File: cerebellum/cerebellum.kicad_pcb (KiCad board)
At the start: 4 copper layers, 95 x 56 mm, 30 parts, among them J1 GPIO, J2 MOTA, J3 MOTB, J4 MD_POW, J5 Conn_SPI, J6 Conn_UART, J7 Conn_I2C, J8 VBUS(OUT), J9 3V3(OUT), SW1 PULLUP, SW2 PULLDOWN, SW3 SW_SPDT, U2 POLOLU_TB6612_CARRIER, U3 HC-SR04

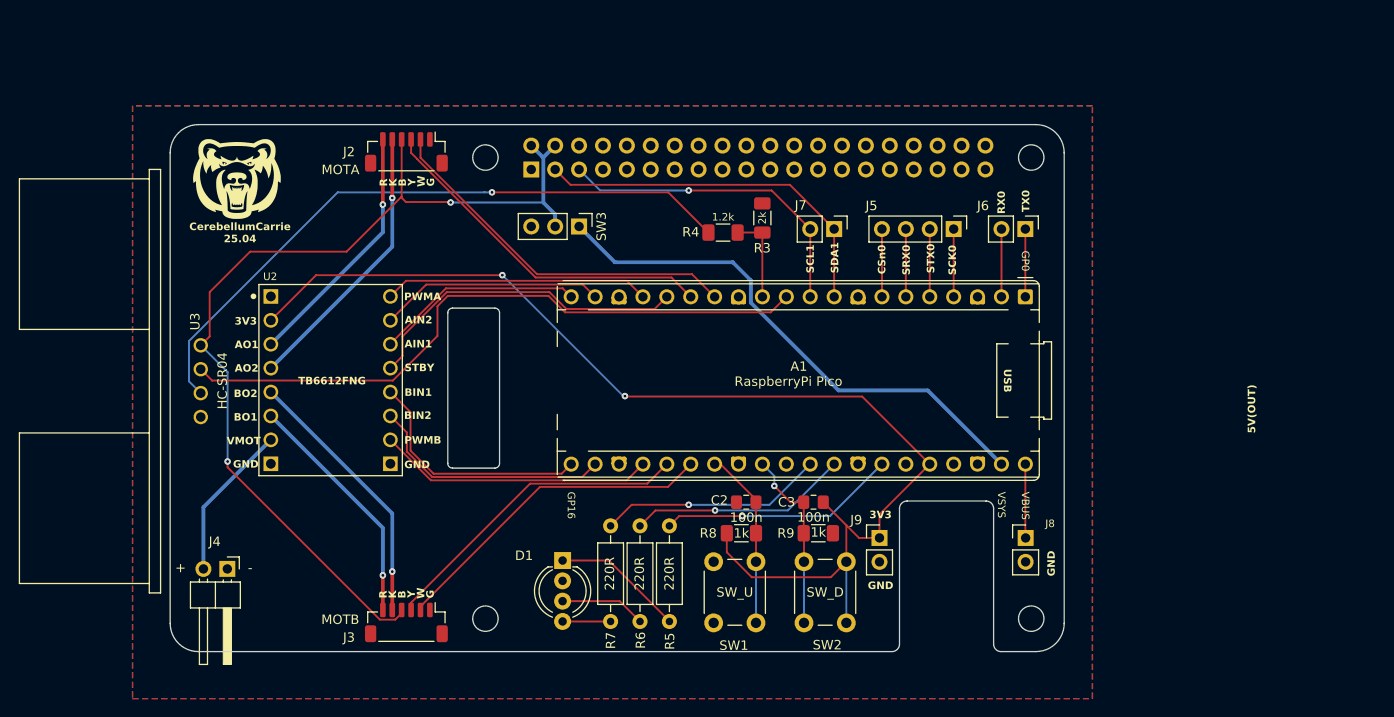
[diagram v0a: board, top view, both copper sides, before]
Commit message: update resistors and capacitors footprint to tht
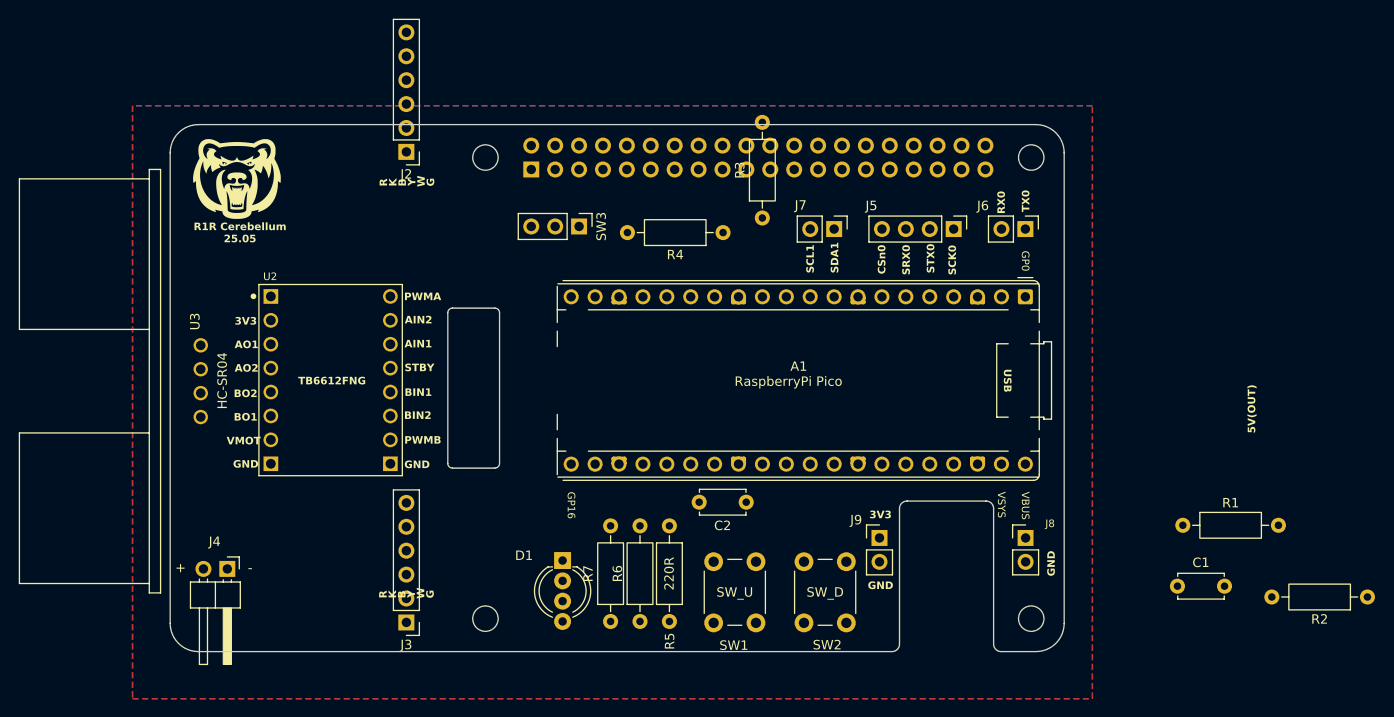
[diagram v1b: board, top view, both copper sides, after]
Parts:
- removed C3: 100n, Capacitor_SMD:C_0805_2012Metric_Pad1.18x1.45mm_HandSolder
- removed R8, R9: 1k, Resistor_SMD:R_1206_3216Metric_Pad1.30x1.75mm_HandSolder
- added C1: 100n, Capacitor_THT:C_Disc_D4.7mm_W2.5mm_P5.00mm, F.Cu at (177.0, 93.0)
- added R1: 1.2k, Resistor_THT:R_Axial_DIN0207_L6.3mm_D2.5mm_P10.16mm_Horizontal, F.Cu at (177.6, 86.6)
- added R2: 2k, Resistor_THT:R_Axial_DIN0207_L6.3mm_D2.5mm_P10.16mm_Horizontal, F.Cu at (197.2, 94.2)
- C2: footprint Capacitor_SMD:C_0805_2012Metric_Pad1.18x1.45mm_HandSolder -> Capacitor_THT:C_Disc_D4.7mm_W2.5mm_P5.00mm
- J2: value MOTA -> Conn_01x06_Pin; footprint Connector_JST:JST_SH_BM06B-SRSS-TB_1x06-1MP_P1.00mm_Vertical -> Connector_PinHeader_2.54mm:PinHeader_1x06_P2.54mm_Vertical
- J3: value MOTB -> Conn_01x06_Pin; footprint Connector_JST:JST_SH_BM06B-SRSS-TB_1x06-1MP_P1.00mm_Vertical -> Connector_PinHeader_2.54mm:PinHeader_1x06_P2.54mm_Vertical
- R3: value 2k -> 220R; footprint Resistor_SMD:R_1206_3216Metric_Pad1.30x1.75mm_HandSolder -> Resistor_THT:R_Axial_DIN0207_L6.3mm_D2.5mm_P10.16mm_Horizontal
- R4: value 1.2k -> 220R; footprint Resistor_SMD:R_1206_3216Metric_Pad1.30x1.75mm_HandSolder -> Resistor_THT:R_Axial_DIN0207_L6.3mm_D2.5mm_P10.16mm_Horizontal
- R6, R7: value 220R -> 1k
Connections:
- C2 pad 1: /SW_PU -> PICO3.3
- C2 pad 2: GND -> /SW_PD
- J2 pad 1: GND -> /AO1
- J2 pad 2: /AENC_W -> /AO2
- J2 pad 3: /AENC_Y -> +5V
- J2 pad 4: +5V -> /AENC_Y
- J2 pad 5: /AO2 -> /AENC_W
- J2 pad 6: /AO1 -> GND
- J3 pad 1: GND -> /BO1
- J3 pad 2: /BENC_W -> /BO2
- J3 pad 3: /BENC_Y -> +5V
- J3 pad 4: +5V -> /BENC_Y
- J3 pad 5: /BO2 -> /BENC_W
- J3 pad 6: /BO1 -> GND
- R3 pad 1: /ECHO -> Net-(D1-RA)
- R3 pad 2: GND -> /R_LED
- R4 pad 1: /ECHO -> Net-(D1-GA)
- R4 pad 2: Net-(U3-ECHO) -> /G_LED
- R5 pad 1: Net-(D1-RA) -> Net-(D1-BA)
- R5 pad 2: /R_LED -> /B_LED
- R6 pad 1: Net-(D1-GA) -> /SW_PU
- R6 pad 2: /G_LED -> PICO3.3
- R7 pad 1: Net-(D1-BA) -> GND
- R7 pad 2: /B_LED -> /SW_PD
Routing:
- net PICO3.3: track 124.8 -> 0.00 mm, vias 2 -> 0
- net +5V: track 103.6 -> 0.00 mm, vias 2 -> 0
- net /TRIG: track 69.7 -> 0.00 mm
- net Net-(U3-ECHO): track 69.6 -> 0.00 mm, vias 1 -> 0
- net VSYS: track 56.7 -> 0.00 mm
- net /SDA: track 39.5 -> 0.00 mm
- net /AENC_W: track 39.3 -> 0.00 mm
- net /AENC_Y: track 37.5 -> 0.00 mm
- net /BENC_W: track 35.4 -> 0.00 mm
- net /STBY: track 35.2 -> 0.00 mm
- net /SCL: track 34.4 -> 0.00 mm, vias 1 -> 0
- net /BENC_Y: track 34.0 -> 0.00 mm
- net /AO2: track 29.6 -> 0.00 mm, vias 1 -> 0
- net /PWMB: track 29.3 -> 0.00 mm
- net /BO2: track 28.5 -> 0.00 mm, vias 1 -> 0
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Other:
- board text added: "R1R Cerebellum 25.05"
- board text removed: "CerebellumCarrie 25.04"

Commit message: update pcb layout
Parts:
- moved R2 79.8 mm to (128.9, 53.1)
- moved R1 57.2 mm to (128.8, 56.8), turned to 180 degrees
- moved C1 55.0 mm to (122.7, 84.5), turned to 180 degrees
- moved R3 44.4 mm to (100.7, 84.5), turned to 0 degrees
- moved R4 42.9 mm to (100.7, 88.0), turned to 0 degrees
- moved R7 26.3 mm to (141.9, 89.1), turned to 180 degrees
- moved R5 23.0 mm to (100.7, 91.2), turned to 0 degrees
- moved D1 17.4 mm to (95.3, 84.6)
- moved SW1 12.6 mm to (120.1, 93.7), turned to 0 degrees
- moved J3 11.8 mm to (83.3, 97.9), turned to 90 degrees
- moved J2 11.8 mm to (83.3, 46.1), turned to 90 degrees
- moved SW2 8.58 mm to (138.3, 98.2), turned to 180 degrees
- moved R6 7.98 mm to (117.8, 89.1), turned to 0 degrees
- moved C2 6.74 mm to (137.9, 84.5)
- moved G*** 2.97 mm to (76.1, 52.6)
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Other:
- board text removed: "SW_D"
- board text removed: "SW_U"

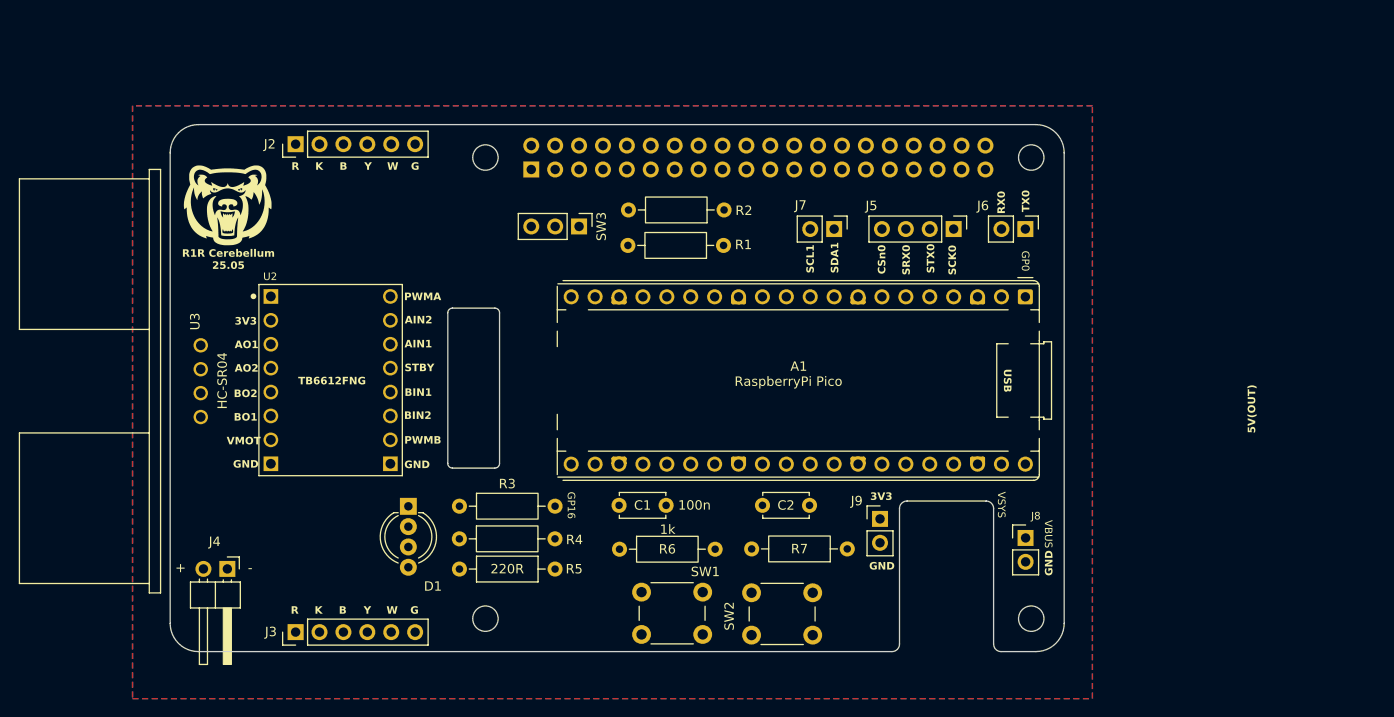
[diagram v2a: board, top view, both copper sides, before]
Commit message: update pcb wiring
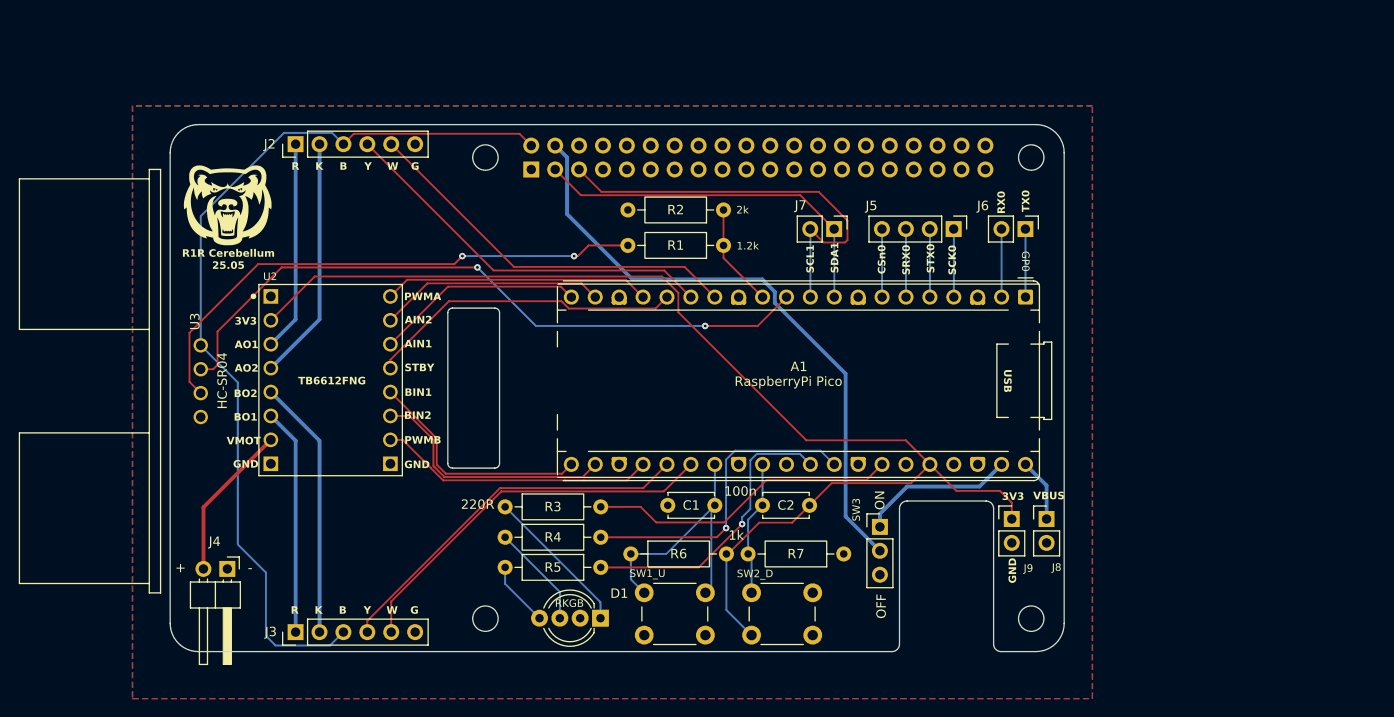
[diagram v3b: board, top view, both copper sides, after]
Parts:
- D1: value LED_RKGB -> RKGB
- SW3: value SW_SPDT -> ON
- moved SW3 45.2 mm to (145.4, 86.8), turned to 0 degrees
- moved D1 23.6 mm to (115.7, 96.5), turned to 180 degrees
- moved J9 14.0 mm to (159.4, 85.9)
- moved C1 5.17 mm to (127.9, 84.5)
- moved R4 4.87 mm to (105.6, 87.8)
- moved R5 4.86 mm to (105.6, 91.0)
- moved R3 4.86 mm to (105.6, 84.6)
- moved J8 3.01 mm to (163.1, 85.9)
- moved R6 1.30 mm to (119.0, 89.6)
- moved R7 0.65 mm to (141.6, 89.6)
- moved SW1_U 0.29 mm to (120.4, 93.8)
- moved R2 0.06 mm to (128.8, 53.1)
- renumbered SW1 to SW1_U, SW2 to SW2_D
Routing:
- net +5V: track 0.00 -> 162.4 mm
- net PICO3.3: track 0.00 -> 128.9 mm
- net /TRIG: track 0.00 -> 72.7 mm, vias 0 -> 2
- net Net-(U3-ECHO): track 0.00 -> 57.3 mm, vias 0 -> 2
- net /SCL: track 0.00 -> 44.7 mm
- net /BENC_W: track 0.00 -> 41.1 mm
- net /AENC_W: track 0.00 -> 41.1 mm
- net /AENC_Y: track 0.00 -> 41.1 mm
- net /BENC_Y: track 0.00 -> 39.9 mm
- net /SDA: track 0.00 -> 39.5 mm
- net /G_LED: track 0.00 -> 33.7 mm, vias 0 -> 1
- net /STBY: track 0.00 -> 33.7 mm
- net /R_LED: track 0.00 -> 33.1 mm
- net /B_LED: track 0.00 -> 31.2 mm, vias 0 -> 1
- net /SW_PU: track 0.00 -> 29.8 mm
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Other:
- board text added: "OFF"
- board text added: "VBUS"
- board text removed: "5V(OUT)"

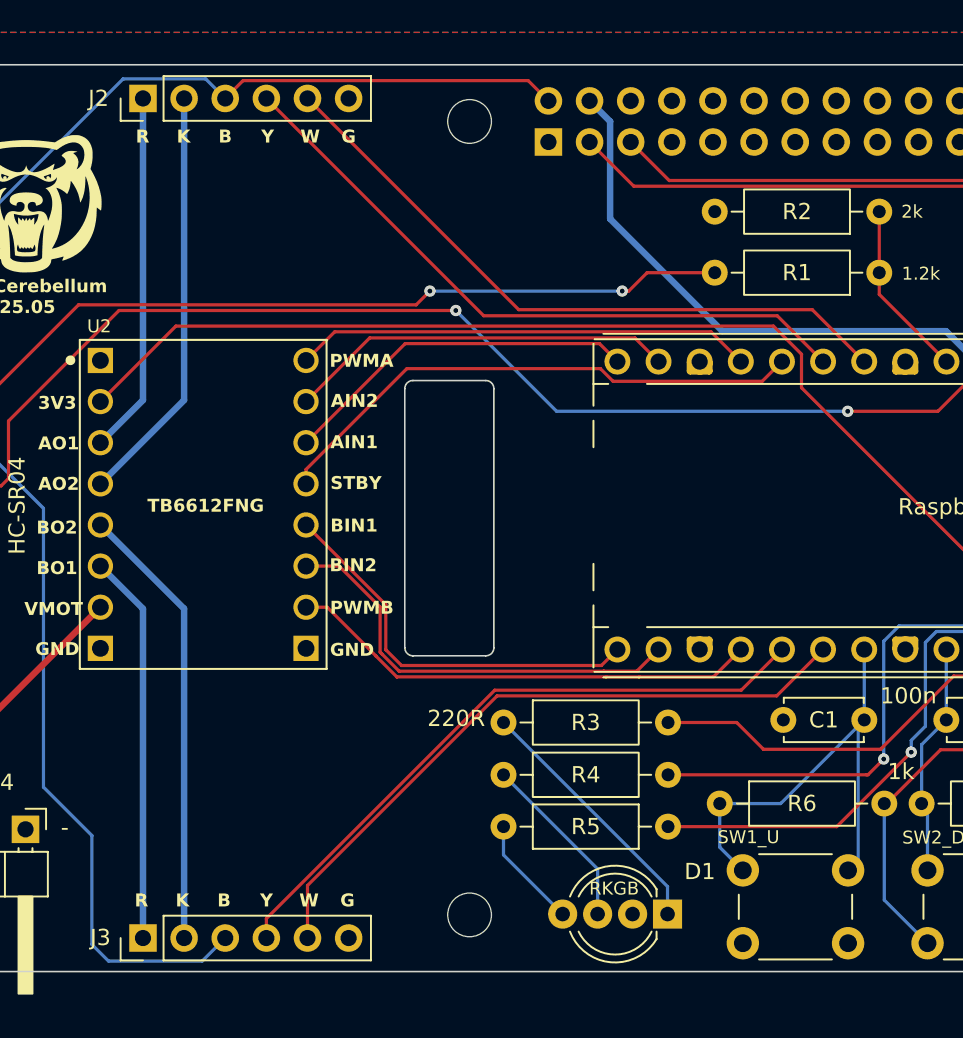
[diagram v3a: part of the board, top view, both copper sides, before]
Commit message: drill two rectangle holes on pcb for motor wiring
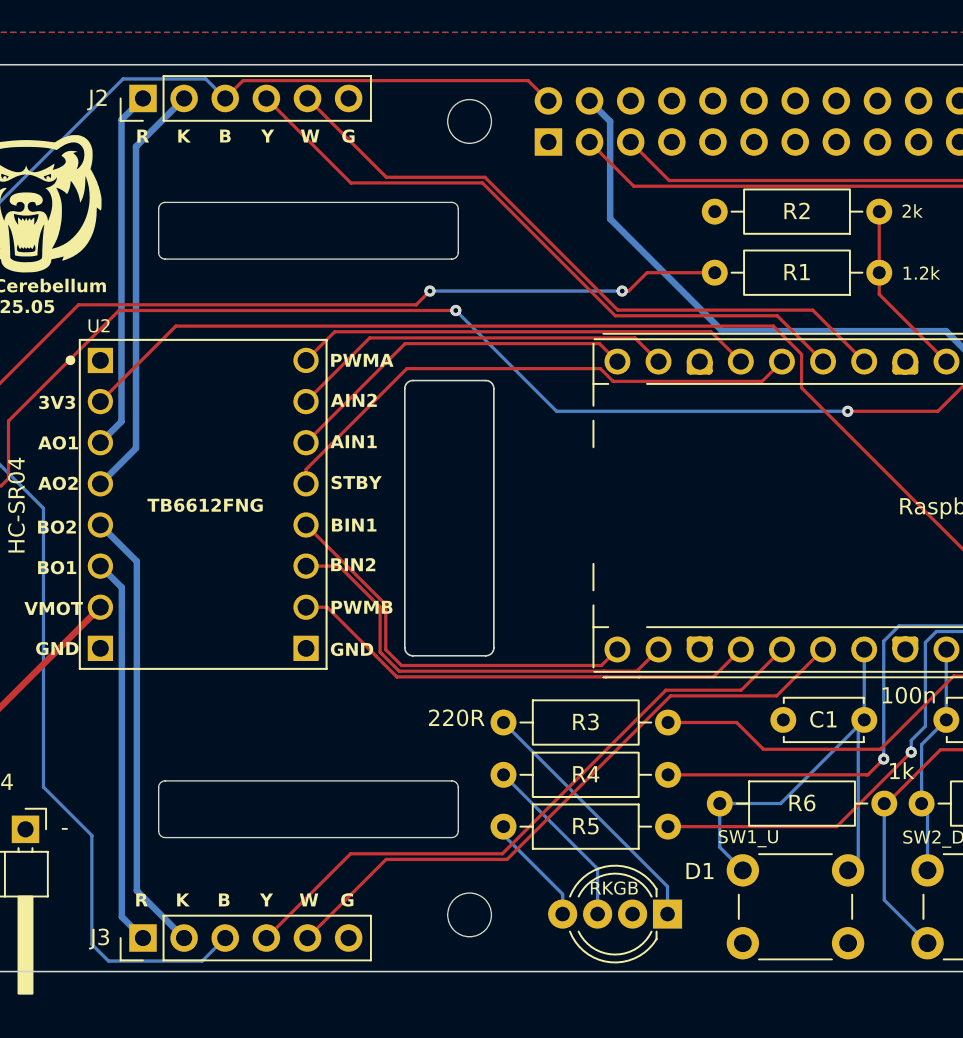
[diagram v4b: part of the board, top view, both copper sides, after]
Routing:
- net /BENC_W: track 41.1 -> 39.2 mm
- net /BENC_Y: track 39.9 -> 39.2 mm
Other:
- outline, holes or cut-outs redrawn

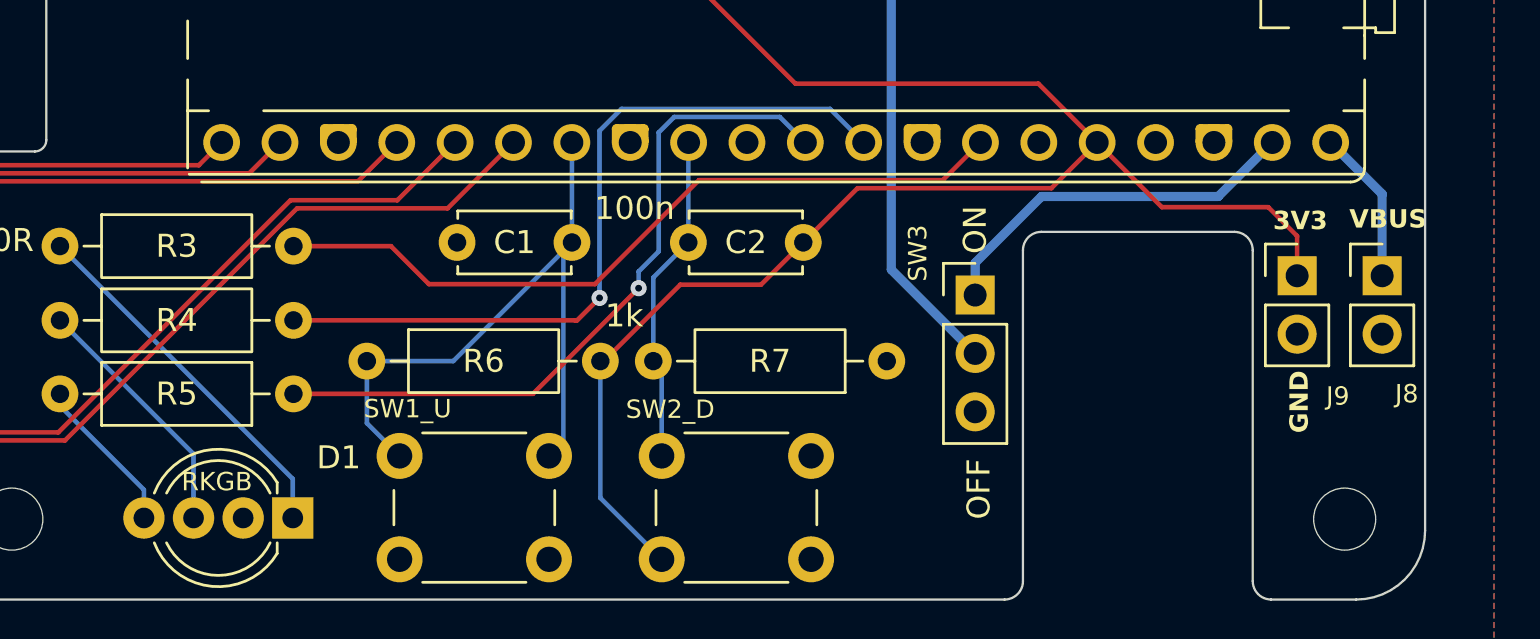
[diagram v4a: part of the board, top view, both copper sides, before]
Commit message: update pico power outlet pins footprint
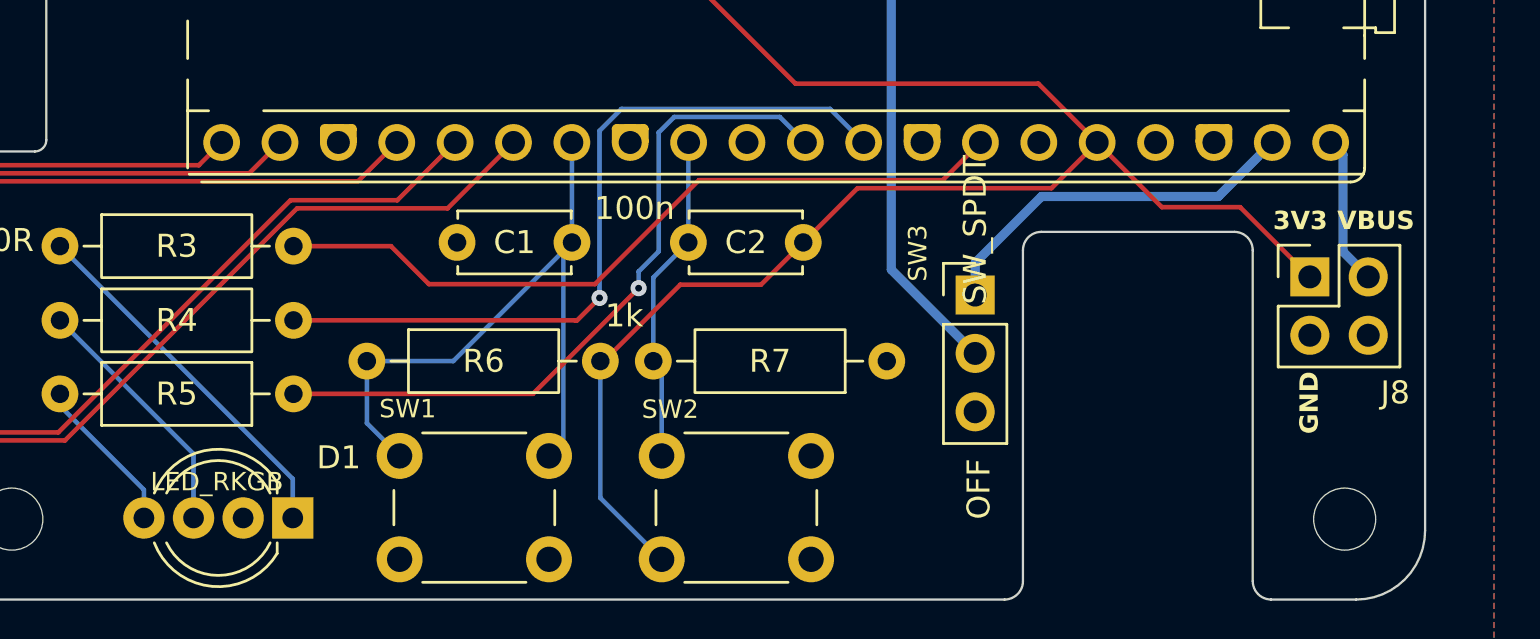
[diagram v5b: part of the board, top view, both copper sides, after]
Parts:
- removed J9: 3V3(OUT), Connector_PinHeader_2.54mm:PinHeader_1x02_P2.54mm_Vertical
- D1: value RKGB -> LED_RKGB
- J8: value VBUS(OUT) -> Conn_02x02_Odd_Even; footprint Connector_PinHeader_2.54mm:PinHeader_1x02_P2.54mm_Vertical -> Connector_PinHeader_2.54mm:PinHeader_2x02_P2.54mm_Vertical
- SW3: value ON -> SW_SPDT
- moved J8 3.15 mm to (160.0, 86.0)
- renumbered SW1_U to SW1, SW2_D to SW2
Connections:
- J8 pad 1: VBUS -> PICO3.3
- J8 pad 2: GND -> VBUS

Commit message: fix pcb
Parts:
- D1: value LED_RKGB -> BGKR
- SW3: value SW_SPDT -> OFF ON
- U3: moved to B.Cu
- turned U3 to 90 degrees
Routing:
- net Net-(U3-ECHO): track 57.3 -> 53.3 mm
- net /TRIG: track 72.7 -> 75.3 mm
- net +5V: track 162.4 -> 163.5 mm
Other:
- board text removed: "OFF"
